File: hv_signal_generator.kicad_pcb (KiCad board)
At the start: 2 copper layers, 83.8 x 56.1 mm, 47 parts, among them J2 COMM_BUS, P3 POWER, P4 VOUT, P5 LIGHT, P6 MAGNET, P7 CONN_01X05, P8 CONN_01X03, Q1 IRF644PBF, Q2 TIP120, Q3 2N7002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

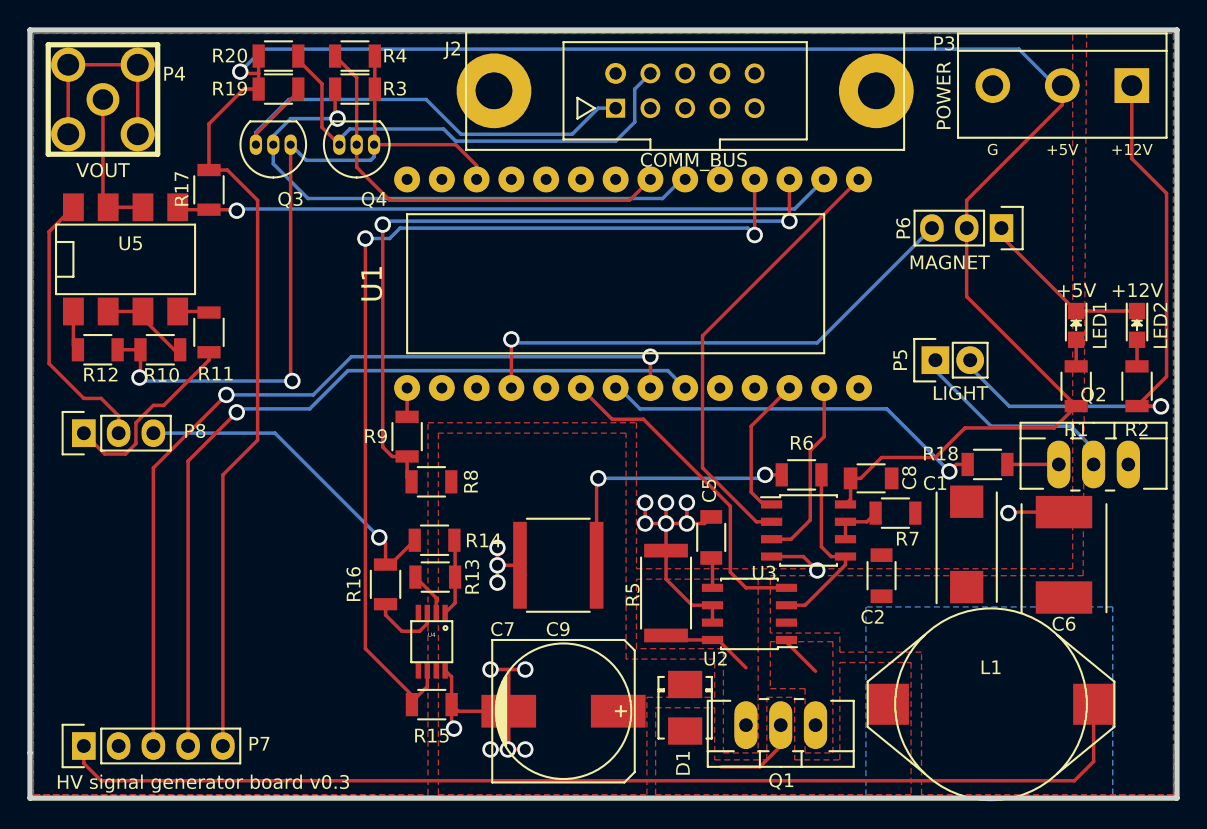
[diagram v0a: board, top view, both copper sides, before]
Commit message: Replace footprint for transistors with SOT-23
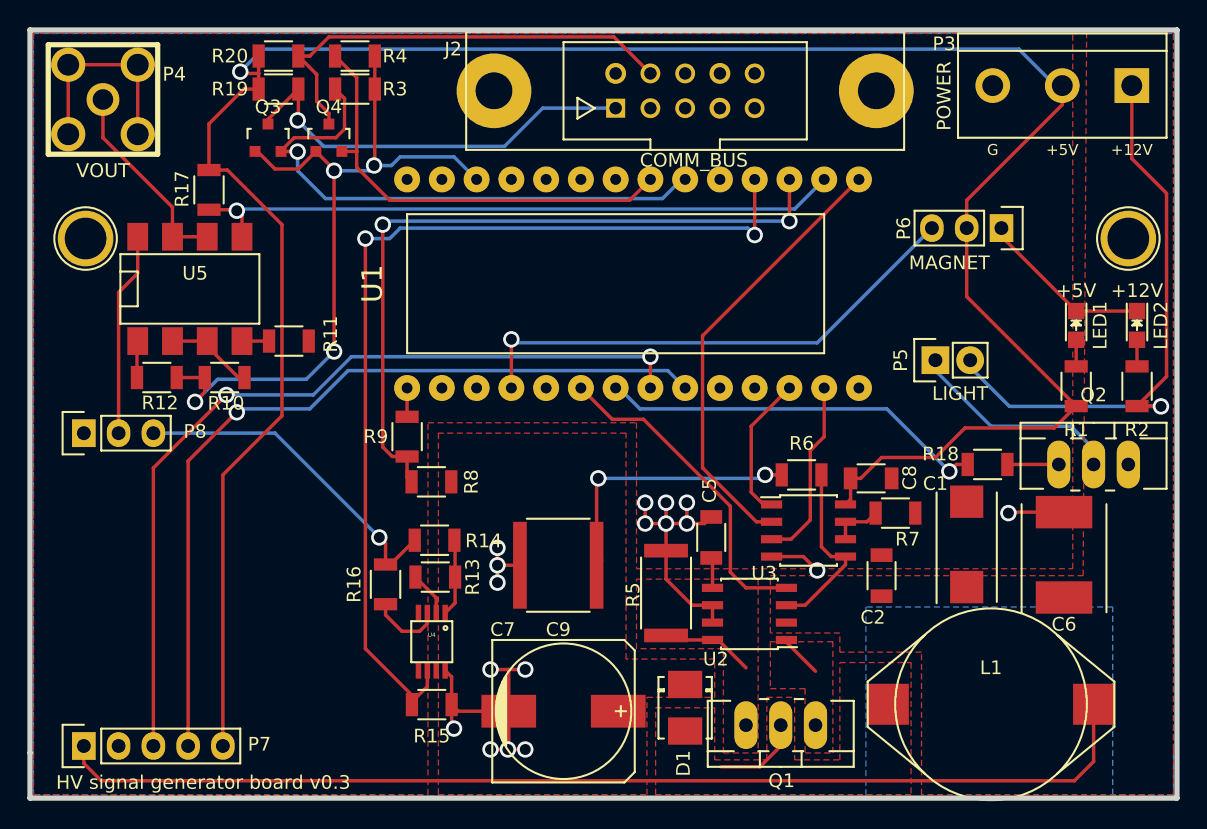
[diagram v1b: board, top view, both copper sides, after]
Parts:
- added REF**: 1pin, Connect:1pin, F.Cu at (20.3, 30.5)
- added REF**: 1pin, Connect:1pin, F.Cu at (96.5, 30.5)
- Q3, Q4: footprint TO_SOT_Packages_THT:TO-92_Inline_Narrow_Oval -> TO_SOT_Packages_SMD:SOT-23
- moved R11 5.88 mm to (35.2, 38.0), turned to 180 degrees
- moved U5 5.17 mm to (27.9, 34.2)
- moved R10 5.12 mm to (30.5, 40.6)
- moved R12 4.77 mm to (25.5, 40.6)
- moved Q4 3.34 mm to (38.1, 23.1), turned to 0 degrees
- moved Q3 1.73 mm to (33.7, 23.1), turned to 0 degrees
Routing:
- net GND: track 98.2 -> 84.1 mm
- net VOUT: track 20.1 -> 15.0 mm
- net SDA_5V: track 35.4 -> 31.2 mm, vias 0 -> 1
- net Net-(P4-Pad1): track 10.6 -> 14.7 mm
- net +5V: track 170.2 -> 171.6 mm
- net SCL_5V: track 35.0 -> 33.6 mm
- net SCL_3.3V: track 31.9 -> 33.0 mm
- net +3.3V: track 55.5 -> 56.1 mm, vias 2 -> 4
